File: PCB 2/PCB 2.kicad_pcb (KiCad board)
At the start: 2 copper layers, 27.5 x 35 mm, 17 parts, among them U1 LM317L_SOT-89, U2 MCP73831T-2ACI_OT

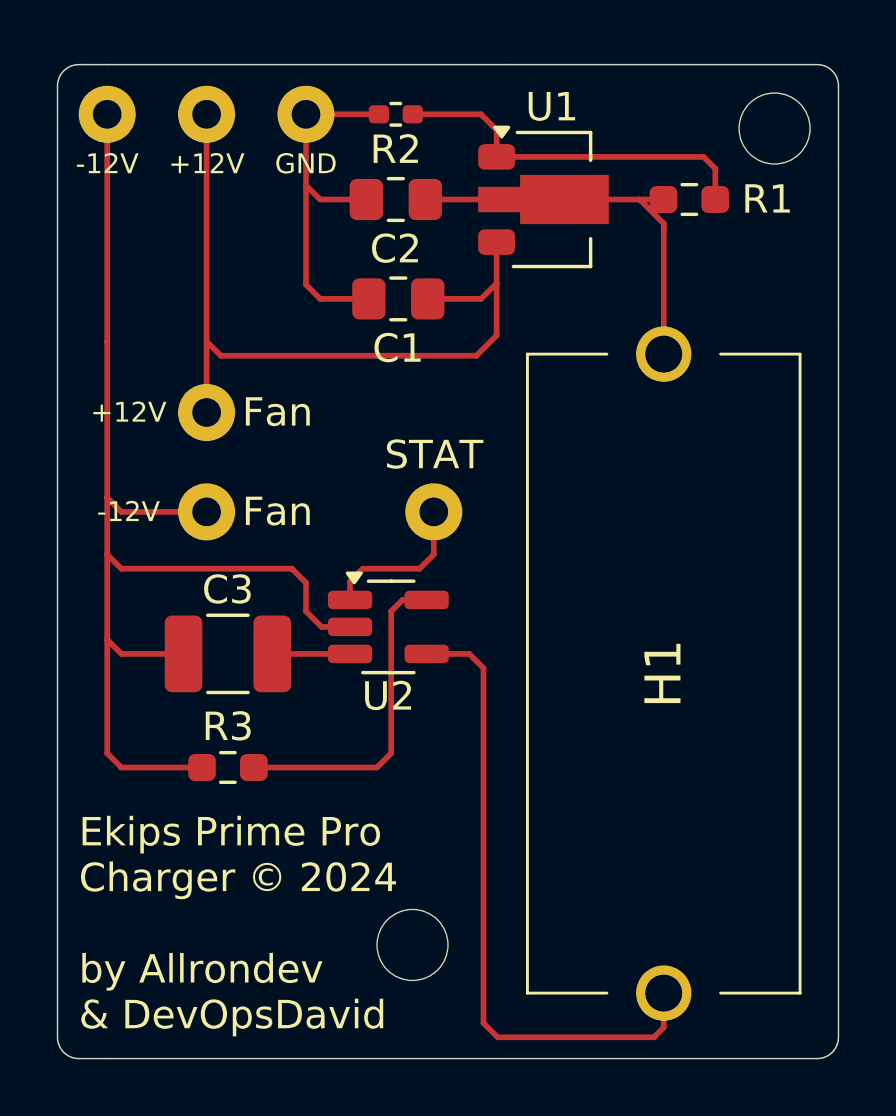
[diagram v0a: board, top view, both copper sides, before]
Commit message: Added Output Pins
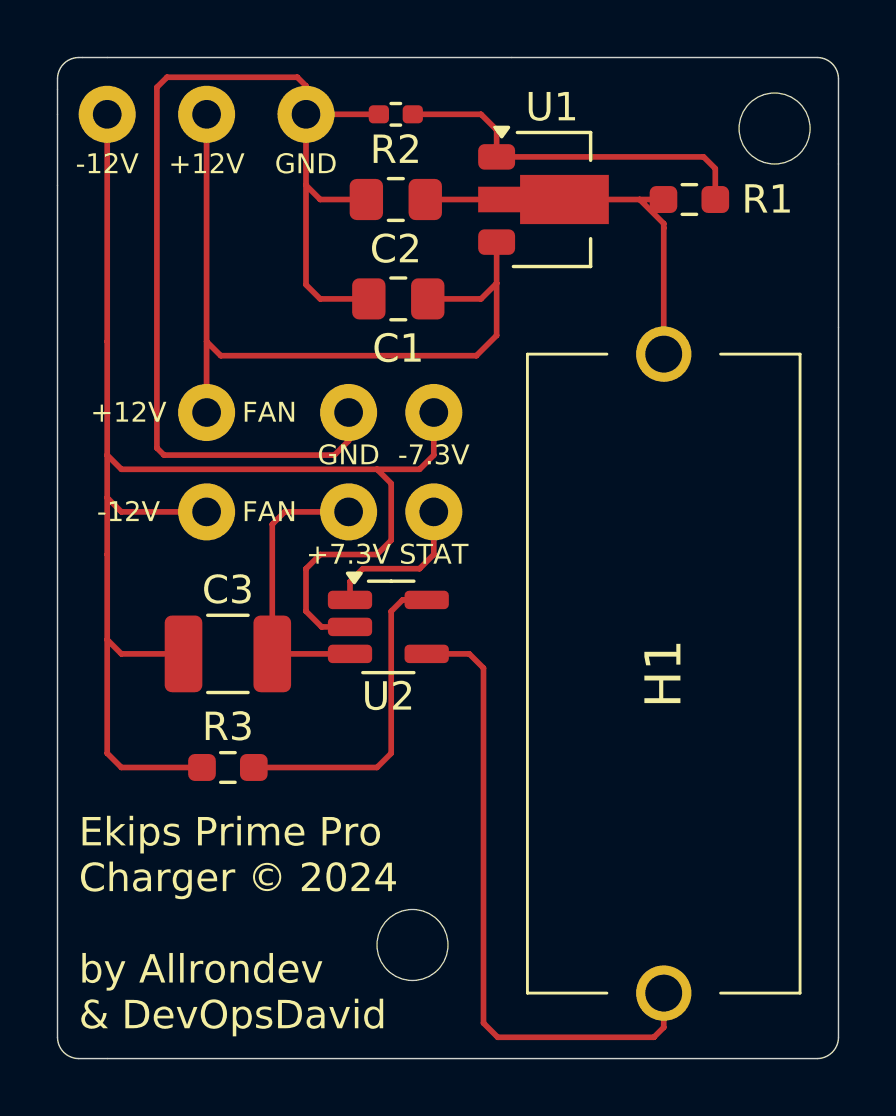
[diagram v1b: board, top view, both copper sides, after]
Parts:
- added ?: , , F.Cu at (25.2, 30.8)
- added ?: , , F.Cu at (25.2, 27.2)
- added ?: , , F.Cu at (28.2, 27.2)
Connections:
- net +12V (VDC) renamed +12V
- net -12V (VDC) renamed -12V (-7.3V)
- net Net-(U1-ADJ) renamed /ADJ
- net Net-(U1-VO) renamed /VO
- net Net-(U2-PROG) renamed /PROG
- net Net-(U2-VBAT) renamed /+7.3V
- net Net-(U2-VDD) renamed /VDD
- ? pad STAT: unconnected-(U2-STAT-Pad1) -> /STAT
- U2 pad 1: unconnected-(U2-STAT-Pad1) -> /STAT
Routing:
- net GND: track 13.3 -> 40.6 mm
- net -12V (-7.3V): track 43.0 -> 55.7 mm
- net /+7.3V: track 2.94 -> 10.4 mm
- net unconnected-(U2-STAT-Pad1): track 5.51 -> 0.00 mm
- net /STAT: track 0.00 -> 5.51 mm
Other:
- board size 27.5 x 35 mm -> 27.5 x 35.2 mm
- board text added: "+7.3V"
- board text added: "-7.3V"
- board text added: "FAN"
- board text removed: "Fan"
